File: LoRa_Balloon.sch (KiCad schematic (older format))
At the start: 13 parts, among them U2 SX1272IMLTRICT-ND_CID104

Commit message: Add files via upload
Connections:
- net labels added: DIO0, DIO1, DIO2, DIO3
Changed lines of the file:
@@
 EESchema Schematic File Version 4
+LIBS:LoRa_Balloon-cache
 EELAYER 30 0
 EELAYER END
@@
 	1575 3250 1975 3250
 Connection ~ 1575 3075
-Text Label 3250 3000 2    35   ~ 7
+Text Label 3250 3000 2    35   ~ 0
 SX1272_RF_RX
 Wire Wire Line
@@
 Wire Wire Line
 	2800 3250 3250 3250
-Text Label 3250 3250 2    35   ~ 7
+Text Label 3250 3250 2    35   ~ 0
 SX1272_RF_TX
 Wire Wire Line
@@
 Wire Wire Line
 	2600 2325 3050 2325
-Text Label 3050 2550 2    35   ~ 7
+Text Label 3050 2550 2    35   ~ 0
 RF_CS
-Text Label 3050 2475 2    35   ~ 7
+Text Label 3050 2475 2    35   ~ 0
 MOSI
-Text Label 3050 2400 2    35   ~ 7
+Text Label 3050 2400 2    35   ~ 0
 MISO
-Text Label 3050 2325 2    35   ~ 7
+Text Label 3050 2325 2    35   ~ 0
 SCK
 $Comp
@@
 	2600 2100 2600 2025
 Connection ~ 2600 2025
-Text Label 2950 1800 2    35   ~ 7
+Text Label 2950 1800 2    35   ~ 0
 RXTX_SW
 $Comp
@@
 	0    1    1    0
 $EndComp
-Text Label 2950 1875 2    35   ~ 7
+Text Label 2950 1875 2    35   ~ 0
 Reset_SX
 Wire Wire Line
@@
 Wire Wire Line
 	2600 1275 2950 1275
-Text Label 2950 1650 2    35   ~ 7
+Text Label 2950 1650 2    35   ~ 0
 DIO5
-Text Label 2950 1575 2    35   ~ 7
+Text Label 2950 1575 2    35   ~ 0
 DIO4
+Text Label 2950 1500 2    35   ~ 0
+DIO3
+Text Label 2950 1425 2    35   ~ 0
+DIO2
+Text Label 2950 1350 2    35   ~ 0
+DIO1
+Text Label 2950 1275 2    35   ~ 0
+DIO0
 $EndSCHEMATC

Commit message: Updated schematic
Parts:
- added C1, C14: C_0402_1.8pF_CID2085, dtusat:C0402, symbol dtusat-capacitors:C_0402_1.8pF_CID2085
- added C11, C19: C_0402_0.5pF_CID2091, dtusat:C0402, symbol dtusat-capacitors:C_0402_0.5pF_CID2091
- added C12, C21: C_0402_10nF_CID2082, dtusat:C0402, symbol dtusat-capacitors:C_0402_10nF_CID2082
- added C13, C24: C_0402_2.4pF_CID2093, dtusat:C0402, symbol dtusat-capacitors:C_0402_2.4pF_CID2093
- added C15, C3: C_0402_20pF_CID2086, dtusat:C0402, symbol dtusat-capacitors:C_0402_20pF_CID2086
- added C16, C6: C_0402_10pF_CID2089, dtusat:C0402, symbol dtusat-capacitors:C_0402_10pF_CID2089
- added C20, C25: C_0402_8.2pF_CID2088, dtusat:C0402, symbol dtusat-capacitors:C_0402_8.2pF_CID2088
- added C22: C_0402_22pF_CID2090, dtusat:C0402, symbol dtusat-capacitors:C_0402_22pF_CID2090
- added C23, C28: C_0402_3.3pF_CID2084, dtusat:C0402, symbol dtusat-capacitors:C_0402_3.3pF_CID2084
- added C26: C_0402_1.5pF_CID2087, dtusat:C0402, symbol dtusat-capacitors:C_0402_1.5pF_CID2087
- added C27, C29: C_0402_1nF_CID2092, dtusat:C0402, symbol dtusat-capacitors:C_0402_1nF_CID2092
- added C30: C_0402_47pF_CID2081, dtusat:C0402, symbol dtusat-capacitors:C_0402_47pF_CID2081
- added C4: C_0805_10uF_CID2079, dtusat:C0805, symbol dtusat-capacitors:C_0805_10uF_CID2079
- added H1: EMI_shield, symbol dtusat-other:EMI_shield
- added J1: COAX, symbol dtusat-other:COAX
- added L1, L5, L6: L_0402_10nH_CID3037, dtusat:L0402, symbol dtusat-inductors:L_0402_10nH_CID3037
- added L3, L7: L_0402_8.2nH_CID3038, dtusat:L0402, symbol dtusat-inductors:L_0402_8.2nH_CID3038
- added L8, L9: L_0402_5.6nH_CID3036, dtusat:L0402, symbol dtusat-inductors:L_0402_5.6nH_CID3036
- added R1, R3: R_0402_6k2_CID1104, dtusat:R0402, symbol dtusat-resistors:R_0402_6k2_CID1104
- added U1, U3: SKY67013-396LF_CID141, dtusat:DFN-8, symbol dtusat-ic:SKY67013-396LF_CID141
- added U4: PE4259_CID105, dtusat:SC70-6, symbol dtusat-ic:PE4259_CID105
- gave numbers to parts that had none: 12
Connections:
- net GND: now also C11.2, C12.2, C14.2, C16.2, C19.2, C20.2, C21.2, C23.2, C27.2, C29.2, C4.2, C6.2, H1.1 (GND), J1.2, U1.9, U3.9, U4.2 (GND)
- net RXTX_SW: now also C29.1, U4.4 (CTRL)
- net SX1272_RF_RX: now also L6.2
- net SX1272_RF_TX: now also C20.1, C22.2
- new net: C22.1, L8.2
- new net: C25.1, C26.2, L8.1, L9.2
- new net: C3.1, L1.2
- new net: L1.1, U1.2 (RF_IN)
- new net: R1.2, U1.1 (VBIAS)
- new net: C13.2, L3.2, U1.7 (RF_OUT/VDD)
- new net: C13.1, C14.1, C15.2
- new net: L5.1, U3.2 (RF_IN)
- new net: C15.1, L5.2
- new net: R3.2, U3.1 (VBIAS)
- new net: C24.2, L7.2, U3.7 (RF_OUT/VDD)
- new net: C30.2, U4.5 (RFC)
- new net: C30.1, J1.1
- new net +3V3: C11.1, C12.1, C16.1, C19.1, C21.1, C27.1, C4.1, C6.1, L3.1, L7.1, R1.1, R3.1, U4.6 (VCC)
- new net LNA2_out: C23.1, C24.1, L6.1
- new net RF_RX: C1.1, C3.2, U4.3 (RF2)
- new net RF_TX: C26.1, C28.1, L9.1, U4.1 (RF1)
- no-connect marks 2 -> 12
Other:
- note added: "Radio"
- note added: "Rx matching - 276.6+j29.7 ohm to 50 ohm"
- note added: "TX matching - 13.5-j7.8 ohm to 50 ohm"
- moved on the sheet: C10, C17, C18, C2, C5, C7, C8, C9, L2, L4, R2, U2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

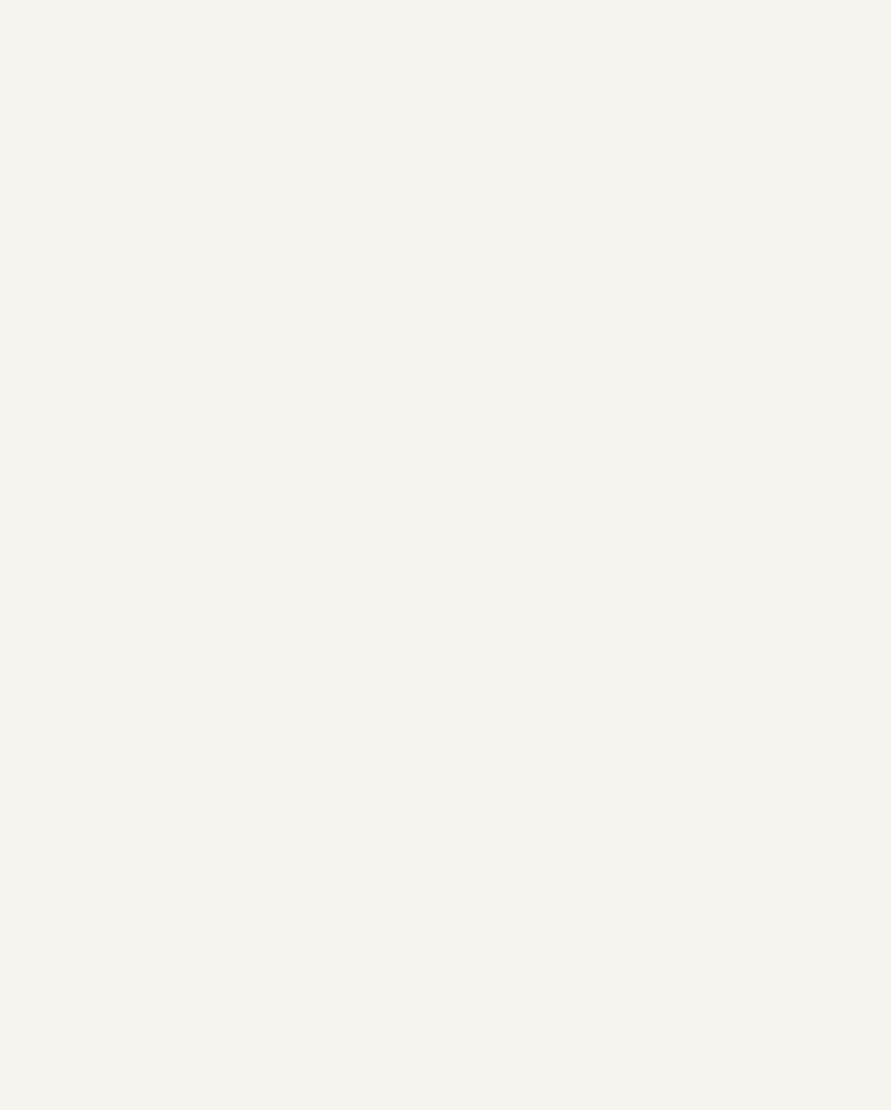
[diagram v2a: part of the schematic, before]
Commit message: Schematics finished
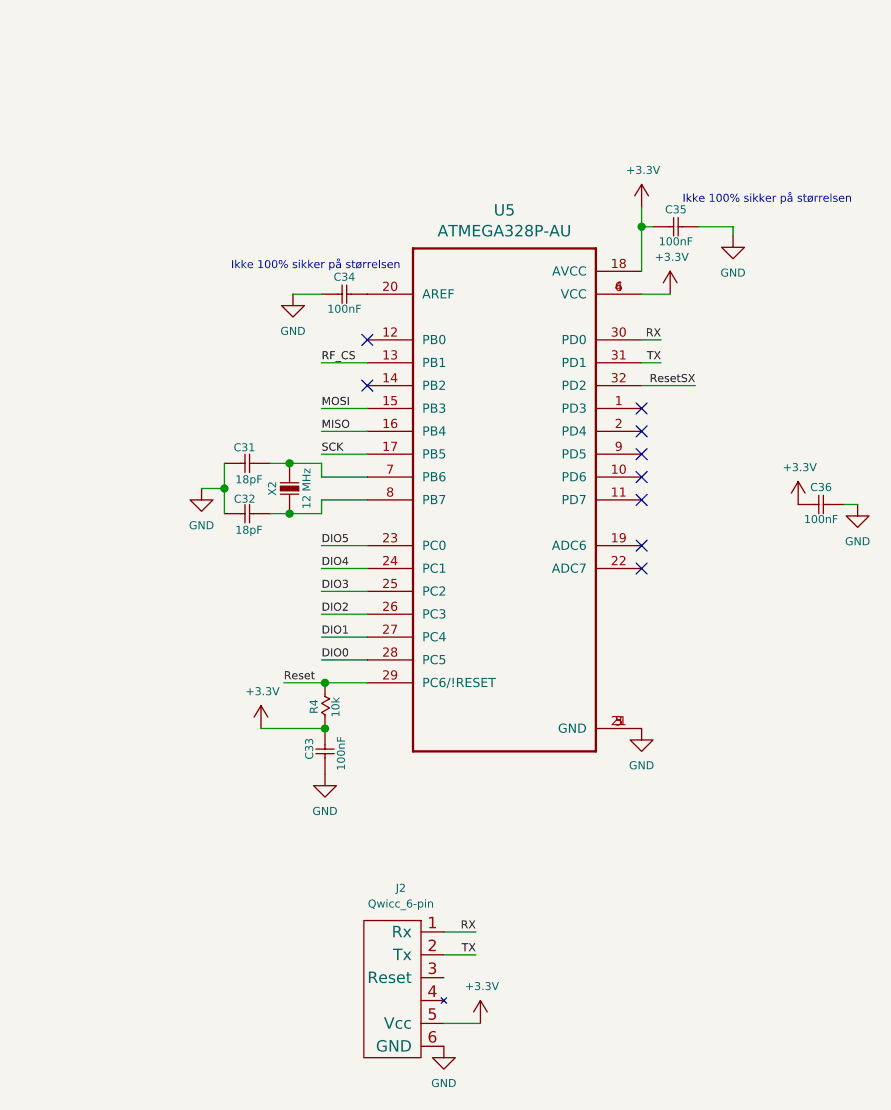
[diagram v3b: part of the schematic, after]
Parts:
- added C31, C32: C_0603_18pF_CID2019, dtusat:C0603, symbol dtusat-capacitors:C_0603_18pF_CID2019
- added C33, C34, C35, C36: C_0402_100nF_CID2072, dtusat:C0402, symbol dtusat-capacitors:C_0402_100nF_CID2072
- added J2: Qwicc_6-pin, dtusat:qwiic_6pin, symbol connectors:Qwicc_6-pin
- added R4: R_0402_10k_CID1101, dtusat:R0402, symbol dtusat-resistors:R_0402_10k_CID1101
- added U5: ATMEGA328P-AU, dtusat:ATMega328P_AU, symbol ATMEGA328P-AU:ATMEGA328P-AU
- added X2: 7A-12.000MAAJ-T_CID117, dtusat:TXC14.3, symbol dtusat-ic:7A-12.000MAAJ-T_CID117
- H1: footprint (none) -> dtusat:BMI-S-203-F_EMI_shield
- J1: footprint (none) -> dtusat:UFL_Feedtrough
- X1: footprint (none) -> dtusat:TSX-3225
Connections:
- net +3V3: now also C33.1, C35.2, C36.2, J2.5 (Vcc), R4.2, U5.18 (AVCC), U5.4 (VCC), U5.6 (VCC)
- net DIO0: now also U5.28 (PC5)
- net DIO1: now also U5.27 (PC4)
- net DIO2: now also U5.26 (PC3)
- net DIO3: now also U5.25 (PC2)
- net DIO4: now also U5.24 (PC1)
- net DIO5: now also U5.23 (PC0)
- net GND: now also C31.1, C32.1, C33.2, C34.2, C35.1, C36.1, J2.6 (GND), U5.21 (GND), U5.3 (GND), U5.5 (GND)
- net MISO: now also U5.16 (PB4)
- net MOSI: now also U5.15 (PB3)
- net RF_CS: now also U5.13 (PB1)
- net SCK: now also U5.17 (PB5)
- new net: C34.1, U5.20 (AREF)
- new net: C31.2, U5.7 (PB6), X2.2
- new net: C32.2, U5.8 (PB7), X2.1
- new net RX: J2.1 (Rx), U5.30 (PD0)
- new net Reset: R4.1, U5.29 (PC6/!RESET)
- new net ResetSX: U5.32 (PD2)
- new net TX: J2.2 (Tx), U5.31 (PD1)
- no-connect marks 12 -> 21
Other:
- note added: "Ikke 100% sikker på størrelsen"

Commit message: PCB finished
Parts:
- removed L2: L_0603_33nH_CID3014, dtusat:L0603, symbol dtusat-inductors:L_0603_33nH_CID3014
- added L2: L_0402_33nH_CID3034, dtusat:L0402, symbol dtusat-inductors:L_0402_33nH_CID3034
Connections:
- net ResetSX is gone; now on net RXTX_SW: U5.32 (PD2)
- net Reset_SX is gone; now on net RXTX_SW: R2.2, U2.6 (Reset)
- net GND: now also C1.2
- net Reset: now also J2.3 (Reset)
- net SX1272_RF_TX: now also L2.1
- net at C2.1, U2.1 (VBAT1): now also C10.1, U2.15 (VBAT2)
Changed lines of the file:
@@
 	1242 1065 1242 1240
 Wire Wire Line
-	1517 990  1042 990
-Wire Wire Line
 	1042 990  1042 1240
-Wire Wire Line
-	1517 915  842  915
 Wire Wire Line
 	842  915  842  1240
@@
 NoConn ~ 2542 1815
 $Comp
-L dtusat-inductors:L_0603_33nH_CID3014 L2
-U 1 1 5DF24B92
-P 2017 2890
-F 0 "L2" V 1974 2889 35  0000 C CNN
-F 1 "L_0603_33nH_CID3014" V 2117 2890 35  0001 C CNN
-F 2 "dtusat:L0603" V 2317 2890 35  0001 C CNN
-F 3 "" H 2017 2890 30  0000 C CNN
-F 4 "33nH" V 2049 2890 35  0000 C CNN "Component value"
-F 5 "3014" V 2167 2890 35  0001 C CNN "CID"
-F 6 "SMD" V 2217 2890 35  0001 C CNN "Technology"
-F 7 "5%" V 2267 2890 35  0001 C CNN "Tolerance"
-	1    2017 2890
-	0    1    1    0
-$EndComp
-$Comp
 L dtusat-inductors:L_0402_2.7nH_CID3035 L4
 U 1 1 5DF26C3D
@@
 Wire Wire Line
 	1517 2890 1517 2715
-Wire Wire Line
-	1517 2890 1917 2890
 Connection ~ 1517 2715
 Text Label 3192 2640 2    35   ~ 0
@@
 	2542 2640 3192 2640
 Wire Wire Line
-	2117 2890 2742 2890
+	2117 2890 2118 2890
 Wire Wire Line
 	2742 2715 2742 2890
@@
 Reset_SX
 Wire Wire Line
-	2542 1440 2892 1440
-Wire Wire Line
-	2542 1515 2892 1515
+	2542 1515 2625 1515
 $Comp
 L dtusat-power:GND #PWR014
@@
 NoConn ~ 9225 2300
 Text Label 9460 2100 2    35   ~ 0
-ResetSX
+RXTX_SW
 Wire Wire Line
 	9225 2100 9460 2100
+$Comp
+L dtusat-power:GND #PWR0101
+U 1 1 5DF275AA
+P 722 3930
+F 0 "#PWR0101" H 722 3680 35  0001 C CNN
+F 1 "GND" H 722 3768 35  0000 C CNN
+F 2 "" H 722 3930 35  0000 C CNN
+F 3 "" H 722 3930 35  0000 C CNN
+	1    722  3930
+	1    0    0    -1
+$EndComp
+$Comp
+L dtusat-inductors:L_0402_33nH_CID3034 L2
+U 1 1 5DF319CF
+P 2018 2890
+F 0 "L2" V 1974 2890 35  0000 C CNN
+F 1 "L_0402_33nH_CID3034" V 2118 2890 35  0001 C CNN
+F 2 "dtusat:L0402" V 2318 2890 35  0001 C CNN
+F 3 "" H 2018 2890 30  0000 C CNN
+F 4 "33nH" V 2052 2890 35  0000 C CNN "Component value"
+F 5 "3034" V 2168 2890 35  0001 C CNN "CID"
+F 6 "SMD" V 2218 2890 35  0001 C CNN "Technology"
+F 7 "2nH" V 2268 2890 35  0001 C CNN "Tolerance"
+	1    2018 2890
+	0    1    1    0
+$EndComp
+Connection ~ 2118 2890
+Wire Wire Line
+	2118 2890 2742 2890
+Wire Wire Line
+	1517 2890 1917 2890
+Wire Wire Line
+	2542 1440 2625 1440
+Wire Wire Line
+	2625 1515 2625 1440
+Connection ~ 2625 1515
+Wire Wire Line
+	2625 1515 2892 1515
+Connection ~ 2625 1440
+Wire Wire Line
+	2625 1440 2892 1440
+Text Label 8500 4690 2    35   ~ 0
+Reset
+Wire Wire Line
+	8360 4690 8500 4690
+Wire Wire Line
+	1517 990  1042 990
+Wire Wire Line
+	842  915  1442 915
+$Comp
+L dtusat-power:+3.3V #PWR?
+U 1 1 5E0E5CD7
+P 1443 914
+F 0 "#PWR?" H 1443 764 35  0001 C CNN
+F 1 "+3.3V" H 1450 1076 35  0000 C CNN
+F 2 "" H 1443 914 35  0000 C CNN
+F 3 "" H 1443 914 35  0000 C CNN
+	1    1443 914
+	1    0    0    -1
+$EndComp
+Wire Wire Line
+	1442 1140 1442 915
+Connection ~ 1442 1140
+Connection ~ 1442 915
+Wire Wire Line
+	1442 915  1517 915
 $EndSCHEMATC
